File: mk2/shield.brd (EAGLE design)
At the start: 83.8 x 55.9 mm, 49 parts, among them P0 CON_DIL_20, P1 CON_DIL_20, P2 CON_DIL_20, P3 CON_DIL_20, P4 CON_DIL_20, P5 CON_DIL_20

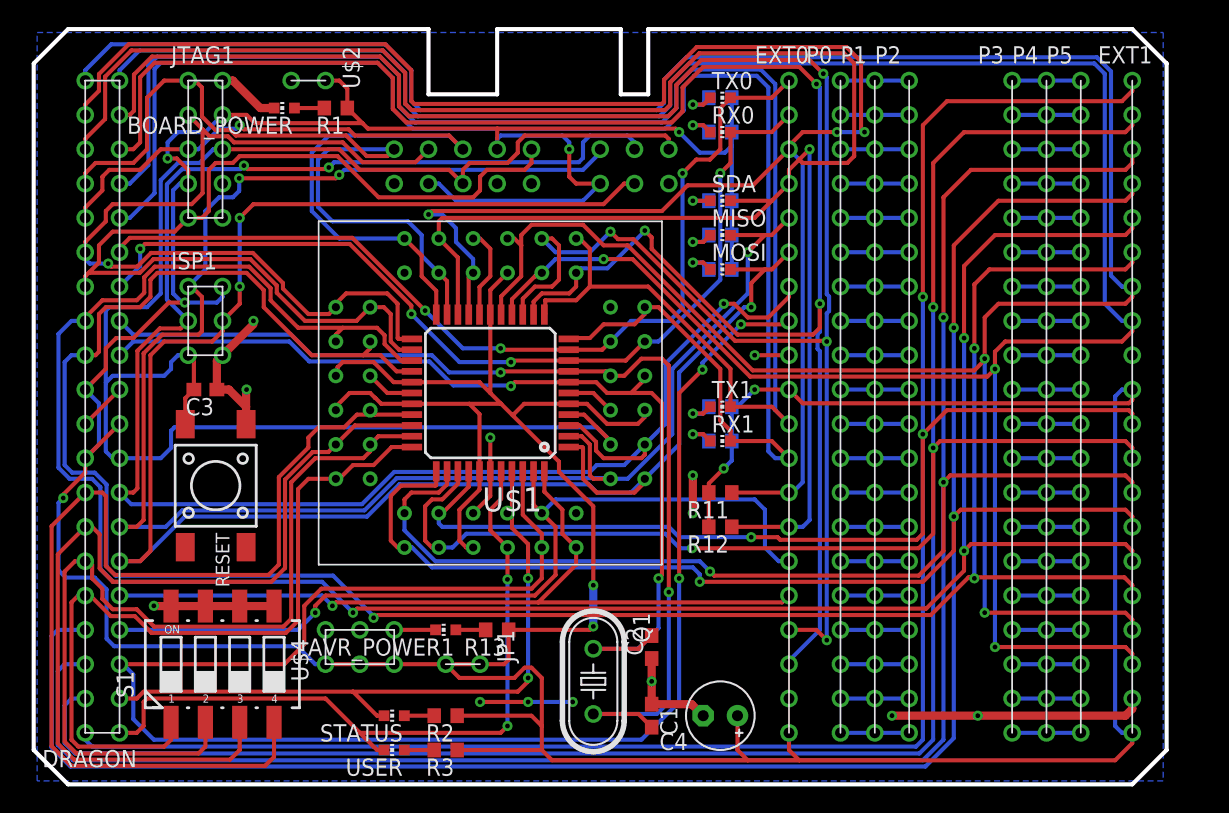
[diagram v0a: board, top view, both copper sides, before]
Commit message: [mega88 led ctrl]
	- add atmega88 controller for interface leds
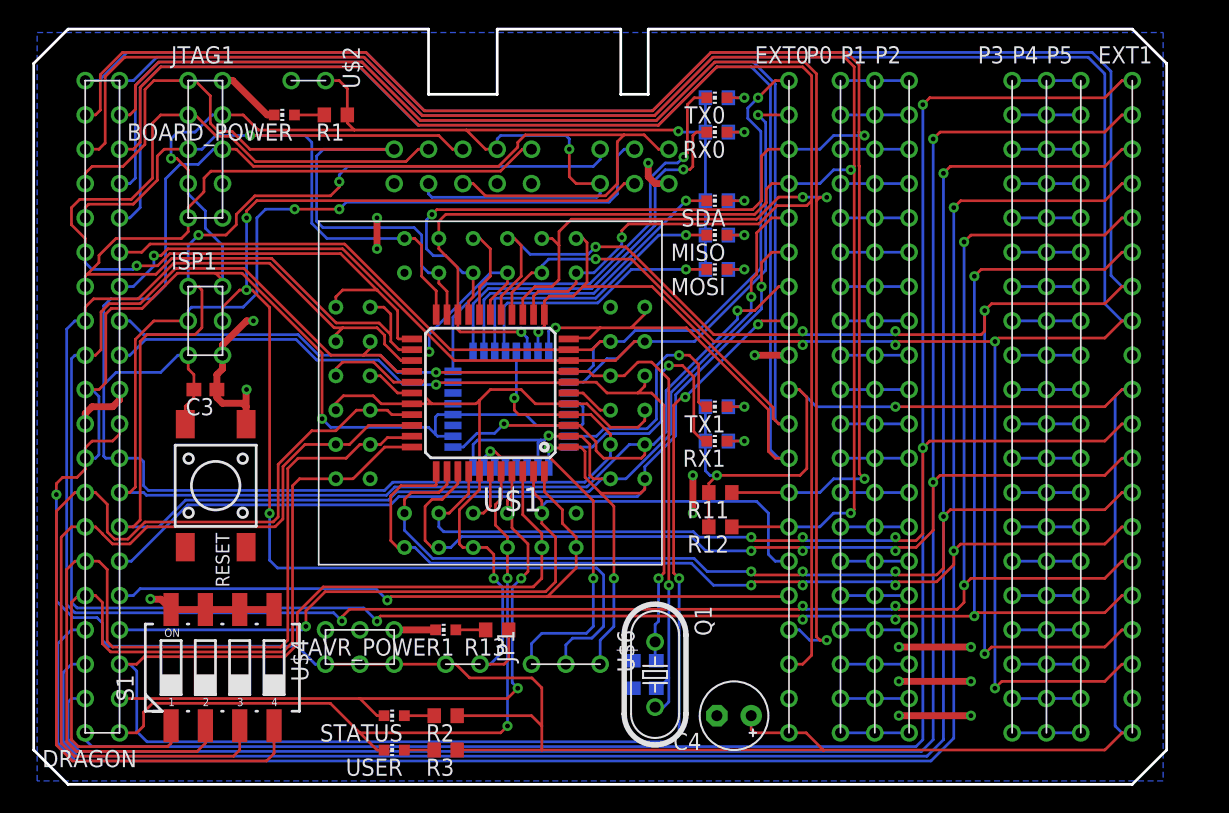
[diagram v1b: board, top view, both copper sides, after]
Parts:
- added U$5: ATMEGA88, mega88:TQFP32-08
- added U$6: CON_DIL_3, connector:CON_DIL_3
- moved Q1 4.60 mm to (44.7, 14.5)
- moved C1 2.09 mm to (43.9, 13.5), flipped to the bottom, turned to 180 degrees
- moved C2 1.14 mm to (43.9, 15.5), flipped to the bottom, turned to 180 degrees
- moved C4 1.02 mm to (50.5, 11.4)
- moved BOARD_POWER 0.51 mm to (17.3, 55.9)
- moved R1 0.51 mm to (21.1, 55.9)
- moved S1 0.25 mm to (12.7, 15.0)
- moved MISO 0.25 mm to (49.3, 47.0), turned to 90 degrees
- moved MOSI 0.25 mm to (49.3, 44.5), turned to 90 degrees
- moved R10 0.25 mm to (49.3, 44.5), turned to 180 degrees
- moved R4 0.25 mm to (49.3, 57.1), turned to 180 degrees
- moved R5 0.25 mm to (49.3, 54.6), turned to 180 degrees
- moved R6 0.25 mm to (49.3, 34.3), turned to 180 degrees
- moved R7 0.25 mm to (49.3, 31.8), turned to 180 degrees
- moved R8 0.25 mm to (49.3, 49.5), turned to 180 degrees
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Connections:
- new net MISO_LED: MISO.C, U$5.27
- new net MOSI_LED: MOSI.C, U$5.28
- new net MOSI_MEGA1284: DRAGON.P$6, EXT0.P$6, U$1.1, U$3.P$1, U$5.9, U$6.P$1
- new net MOSI_MEGA88: U$5.15, U$6.P$3
- new net RX0_LED: RX0.C, U$5.25
- new net RX1_LED: RX1.C, U$5.8
- new net SDA_LED: SDA.C, U$5.26
- new net TX0_LED: TX0.C, U$5.24
- new net TX1_LED: TX1.C, U$5.7
- new net VCC_MEGA1284: JP1.P$1, R13.1, U$1.17, U$1.27, U$1.29, U$1.38, U$1.5, U$3.P$18, U$3.P$29, U$3.P$31, U$3.P$41, U$3.P$5
- net /RESET: now also U$5.29
- net GND: now also U$5.21, U$5.3, U$5.5
- net MISO: now also U$5.10, U$5.16; no longer MISO.C
- net MOSI: now also U$6.P$2; no longer DRAGON.P$6, EXT0.P$6, MOSI.C, U$1.1, U$3.P$1
- net RX0: now also U$5.2; no longer RX0.C
- net RX1: now also U$5.32; no longer RX1.C
- net SCK: now also U$5.17
- net SDA: now also U$5.30; no longer SDA.C
- net TX0: now also U$5.1; no longer TX0.C
- net TX1: now also U$5.31; no longer TX1.C
- net VCC: now also U$5.18, U$5.20, U$5.4, U$5.6; no longer JP1.P$1, R13.1, U$1.17, U$1.27, U$1.29, U$1.38, U$1.5, U$3.P$18, U$3.P$29, U$3.P$31, U$3.P$41, U$3.P$5
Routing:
- net MOSI_MEGA1284: track 0.00 -> 89.2 mm, vias 0 -> 3
- net VCC_MEGA1284: track 0.00 -> 79.4 mm, vias 0 -> 2
- net MOSI: track 137.5 -> 93.4 mm
- net VCC: track 408.9 -> 366.6 mm, vias 9 -> 7
- net TX0_LED: track 0.00 -> 33.6 mm, vias 0 -> 1
- net RX0_LED: track 0.00 -> 29.4 mm, vias 0 -> 1
- net MOSI_MEGA88: track 0.00 -> 26.4 mm, vias 0 -> 2
- net /RESET: track 123.2 -> 147.7 mm, vias 0 -> 1
- net SDA_LED: track 0.00 -> 23.3 mm, vias 0 -> 1
- net MISO_LED: track 0.00 -> 21.5 mm, vias 0 -> 1
- net MOSI_LED: track 0.00 -> 19.5 mm, vias 0 -> 1
- net RX1_LED: track 0.00 -> 19.5 mm, vias 0 -> 1
- net TX1_LED: track 0.00 -> 18.2 mm, vias 0 -> 1
- net GND: track 90.3 -> 78.5 mm, vias 13 -> 15
- net MISO: track 133.0 -> 142.6 mm, vias 3 -> 4
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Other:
- board text added: "MEGA1284"
- board text added: "MEGA88"
- board text added: "PROGRAM"

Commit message: [relocate]
	- make more space on the right side of the board to increase the
	  size of extension boards
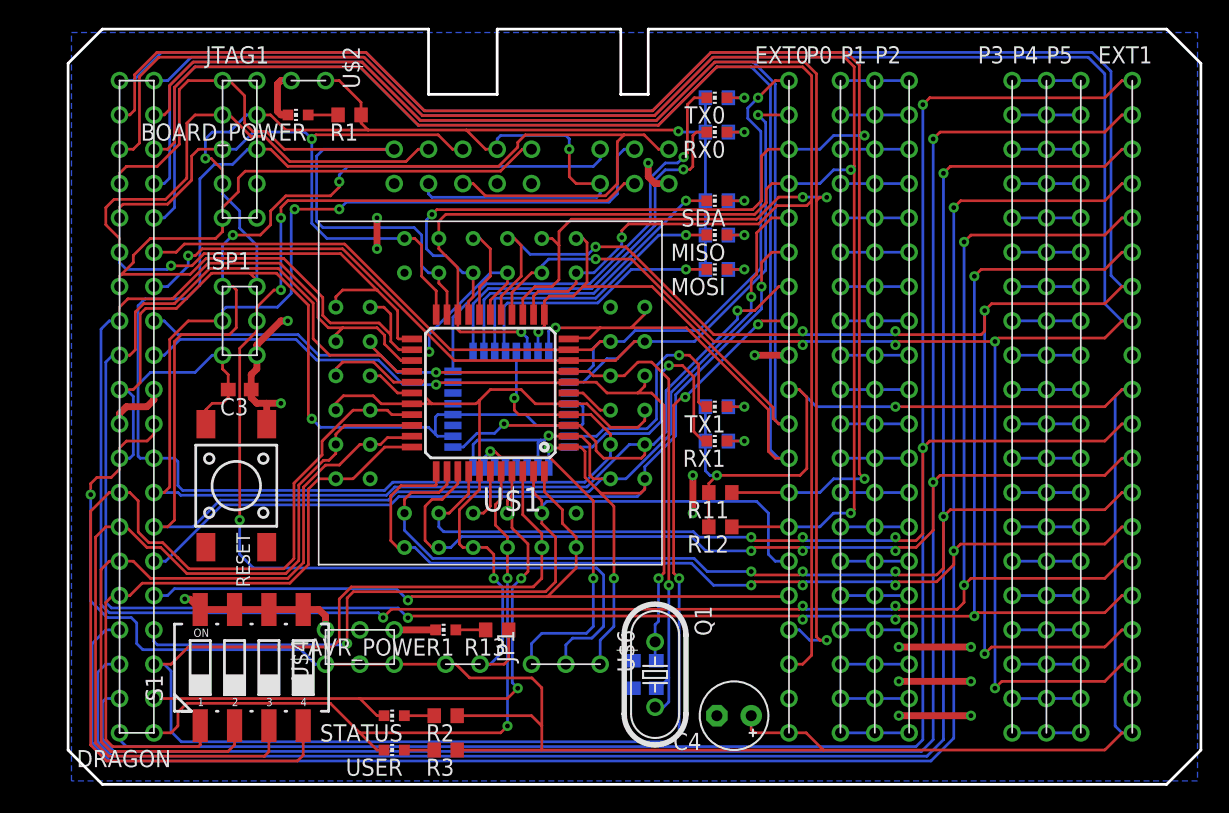
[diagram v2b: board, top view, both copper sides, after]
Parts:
- moved C3 2.54 mm to (14.0, 35.6)
- moved ISP1 2.54 mm to (14.0, 40.6)
- moved JTAG1 2.54 mm to (14.0, 53.3)
- moved DRAGON 2.54 mm to (6.35, 34.3)
- moved S1 2.16 mm to (14.9, 15.0)
- moved RESET 1.52 mm to (13.7, 28.4)
- moved BOARD_POWER 1.02 mm to (18.3, 55.9)
- moved R1 1.02 mm to (22.1, 55.9)
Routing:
- net SW1: track 70.3 -> 55.9 mm
- net SW0: track 61.1 -> 49.5 mm
- net TMS: track 57.5 -> 50.9 mm
- net VCC: track 366.6 -> 361.5 mm
- net TDO: track 70.6 -> 65.5 mm
- net MISO: track 142.6 -> 137.7 mm
- net SCK: track 135.7 -> 130.9 mm
- net TOSC1: track 174.2 -> 169.5 mm
- net AIN0: track 125.9 -> 121.3 mm
- net TDI: track 70.5 -> 66.2 mm
- net /RESET: track 147.7 -> 143.5 mm
- net TOSC2: track 169.9 -> 166.1 mm
- net MOSI: track 93.4 -> 90.3 mm
- net SCL: track 152.7 -> 150.1 mm
- net SDA: track 156.8 -> 154.2 mm
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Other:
- outline, holes or cut-outs redrawn

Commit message: [fix mk2 text size]
	- increase the font size of texts to make the smallest ones readable
	  for the mk2 shield, extension header and ftdiusb extension board
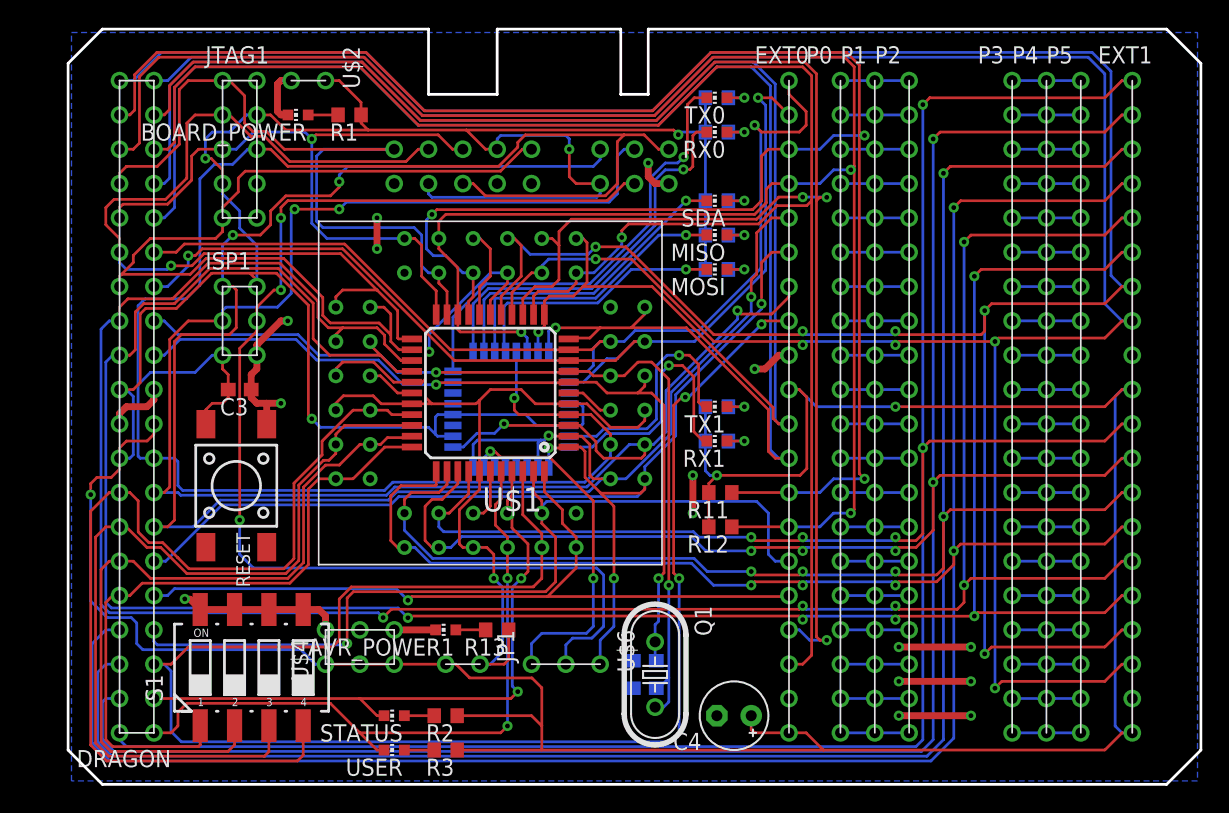
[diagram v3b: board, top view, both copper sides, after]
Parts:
- AVR_POWER1, BOARD_POWER, STATUS: value (none) -> green
- C1, C2: value 22u -> 22p
- C3: value 22u -> 100n
- C4: value (none) -> 100u
- MISO, MOSI, USER: value (none) -> blue
- Q1: value (none) -> 20M
- R1, R13, R2, R4, R5, R6, R7, R8: value (none) -> 220
- R10, R3, R9: value (none) -> 330
- R11, R12: value 1k -> 4.7k
- RX0, RX1, TX0, TX1: value (none) -> red
- SDA: value (none) -> white
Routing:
- net TX0: track 71.8 -> 74.5 mm
- net RX0: track 73.9 -> 75.7 mm
- net SCK: track 130.9 -> 131.6 mm

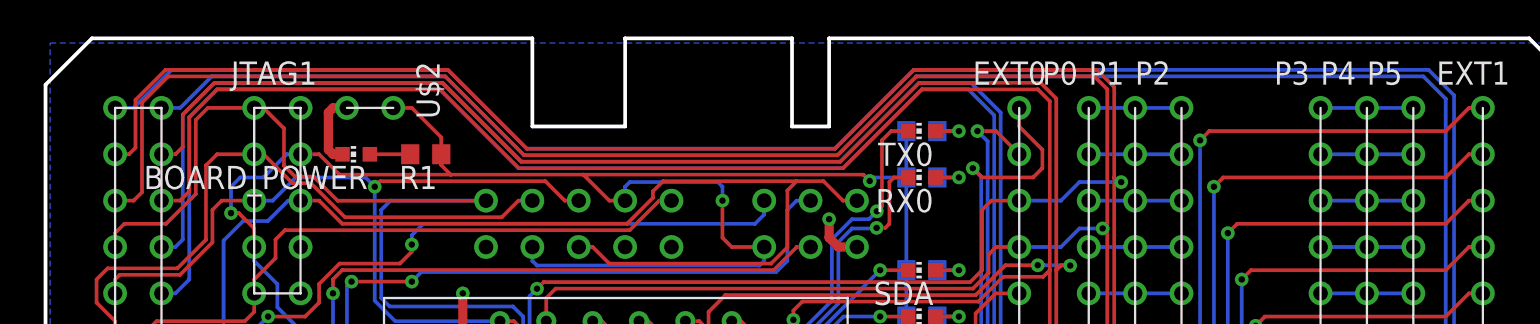
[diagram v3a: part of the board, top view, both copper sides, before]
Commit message: [fix mk2 supply connector]
	- fix the position of the supply power connector since it didn't
	  match the avr dragon header
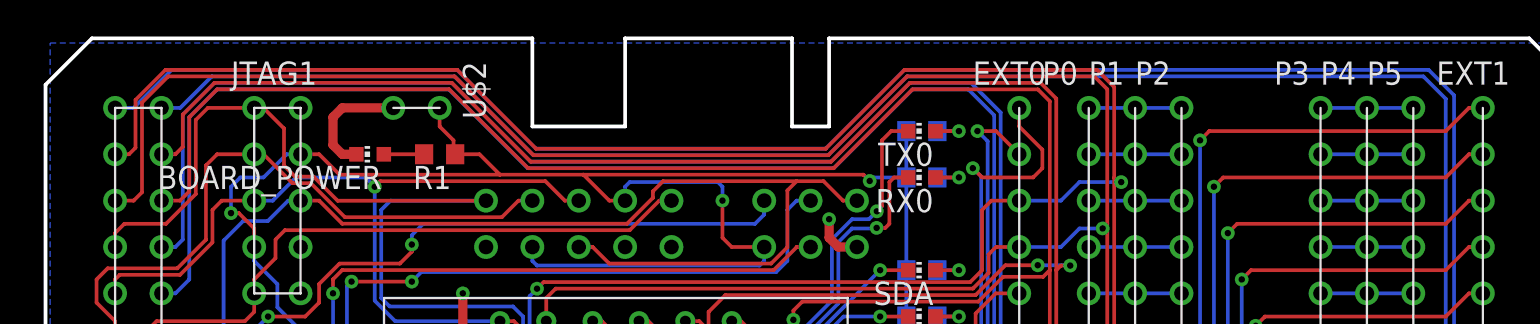
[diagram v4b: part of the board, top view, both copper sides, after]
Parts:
- moved U$2 2.54 mm to (20.3, 58.4)
- moved BOARD_POWER 0.76 mm to (19.1, 55.9)
- moved R1 0.76 mm to (22.9, 55.9)
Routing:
- net GND: track 79.4 -> 81.9 mm

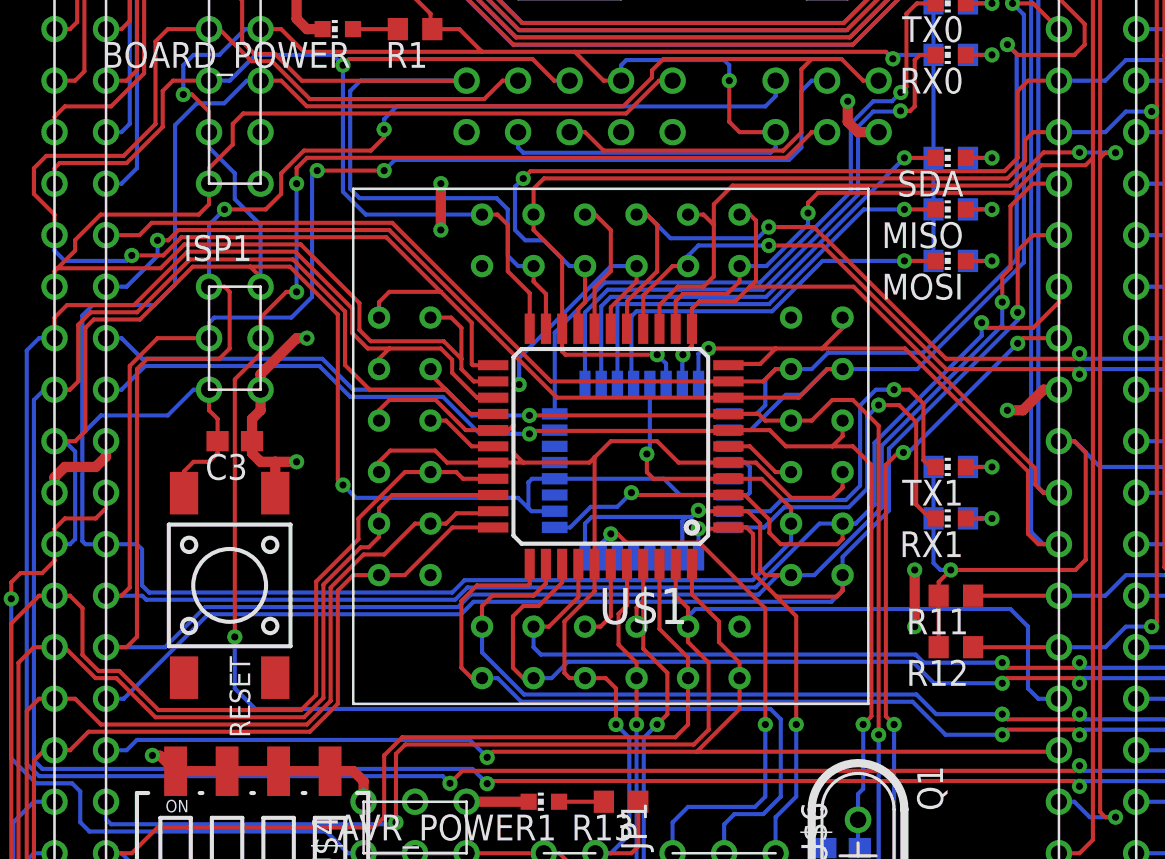
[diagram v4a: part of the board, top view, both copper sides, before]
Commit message: [fix atmega1284p adapter drill size]
	- extend the drill size of the atmega1284p adapter
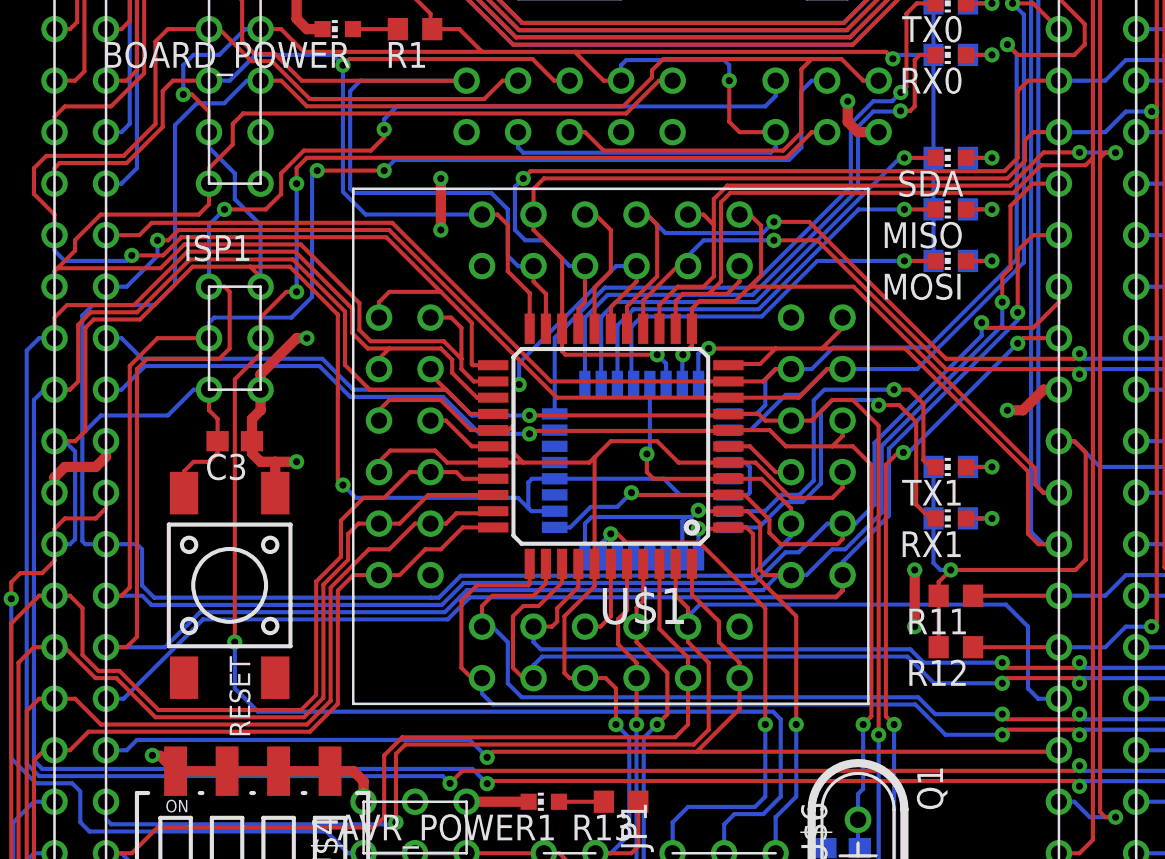
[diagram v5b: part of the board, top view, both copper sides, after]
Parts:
- U$3: device 1284p.rpt:TQFP44-ADAPTER -> mega1284p:TQFP44-ADAPTER
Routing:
- net OC1B: track 128.2 -> 131.9 mm, vias 1 -> 0
- net STATUS_LED: track 48.3 -> 47.2 mm
- net MISO_LED: track 21.5 -> 20.9 mm
- net ADC1: track 191.5 -> 192.1 mm

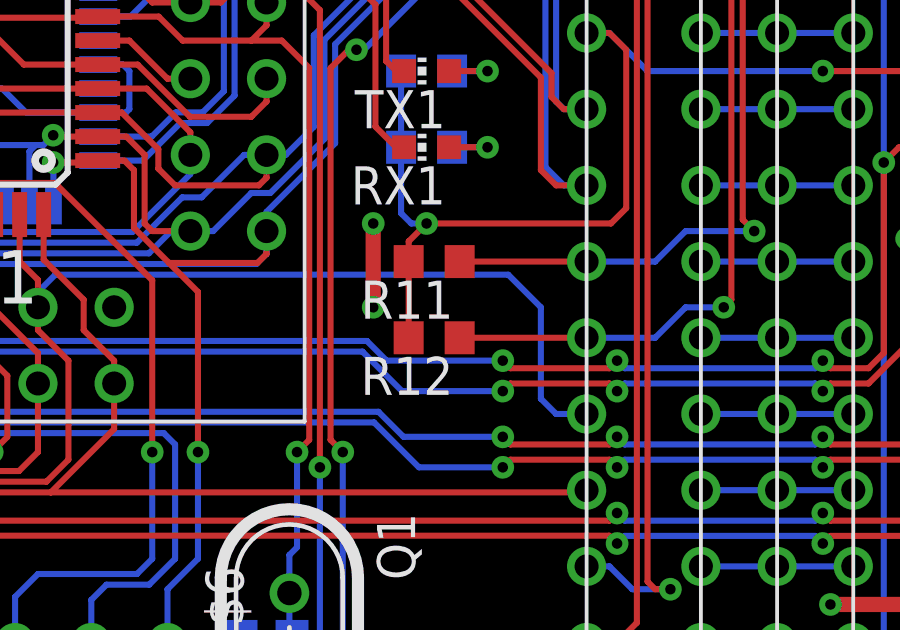
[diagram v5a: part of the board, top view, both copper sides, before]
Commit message: [update fonts]
	- change the size and font of board texts
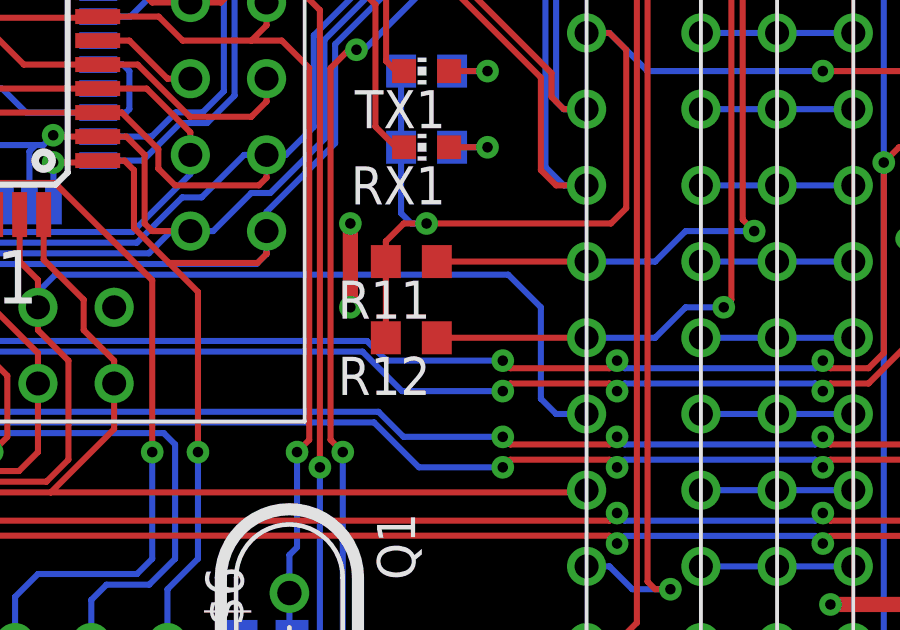
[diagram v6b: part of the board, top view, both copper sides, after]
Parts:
- moved R11 0.76 mm to (48.8, 27.9)
- moved R12 0.76 mm to (48.8, 25.4)
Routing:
- net VCC: track 361.9 -> 362.6 mm
- net SDA: track 154.2 -> 155.0 mm
- net SCL: track 150.1 -> 150.9 mm
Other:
- board text added: "DRAGON SHIELD MK2.1"
- board text removed: "DRAGON SHIELD MK2"
